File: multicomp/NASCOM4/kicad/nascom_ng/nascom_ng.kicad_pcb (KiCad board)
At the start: 2 copper layers, 170 x 145 mm, 113 parts, among them J1 Conn_02x14_Even_Odd, J10 Conn_01x03_Male, J11 Conn_02x02_Odd_Even, J12 Conn_02x01, J13 Conn_02x02_Odd_Even, J14 Conn_02x08_Odd_Even, J15 Conn_01x04_Male, J16 Conn_01x04_Male, J17 Conn_01x04_Male, J18 Conn_01x04_Male, J2 Conn_02x14_Even_Odd, J3 Conn_02x14_Even_Odd, J4 Conn_02x14_Even_Odd, J5 DB15_Female_HighDensity, J6 DB15_Female_HighDensity, J7 Conn_02x17_Odd_Even, J8 Conn_01x06, J9 Mini-DIN_6pins_ver2, SW1 SW_Push, SW2 SW_Push, SW3 SW_Push, U1 Z80PIO, U10 74HCT244, U11 74LVC244, U12 74LVC244, U13 Z80CTC, U14 74LS38, U15 74LS174, U16 74HCT10, U17 74HCT123, U2 WD2797, U3 74LS06, U4 AS6C4008-55PCN, U5 AS6C4008-55PCN, U6 74LVC245, U7 74LVC244, U8 74LS367, U9 74HCT123

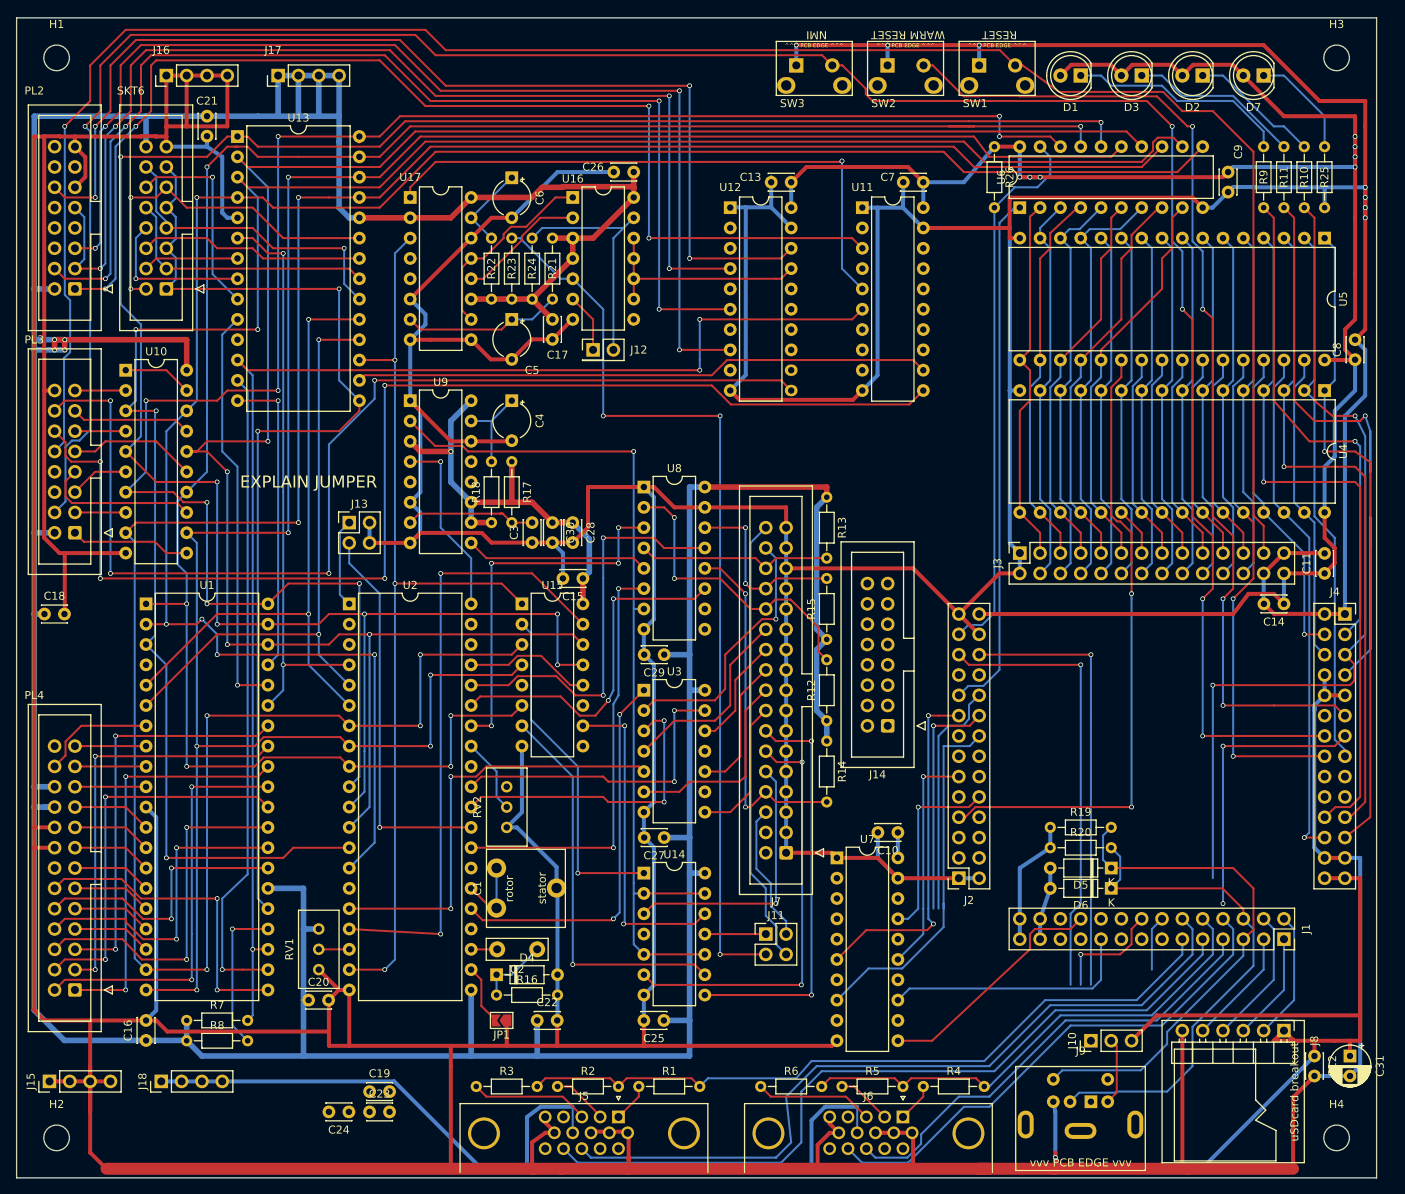
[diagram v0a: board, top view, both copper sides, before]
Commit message: All nets routed, ref designators resequenced, nearly finished!
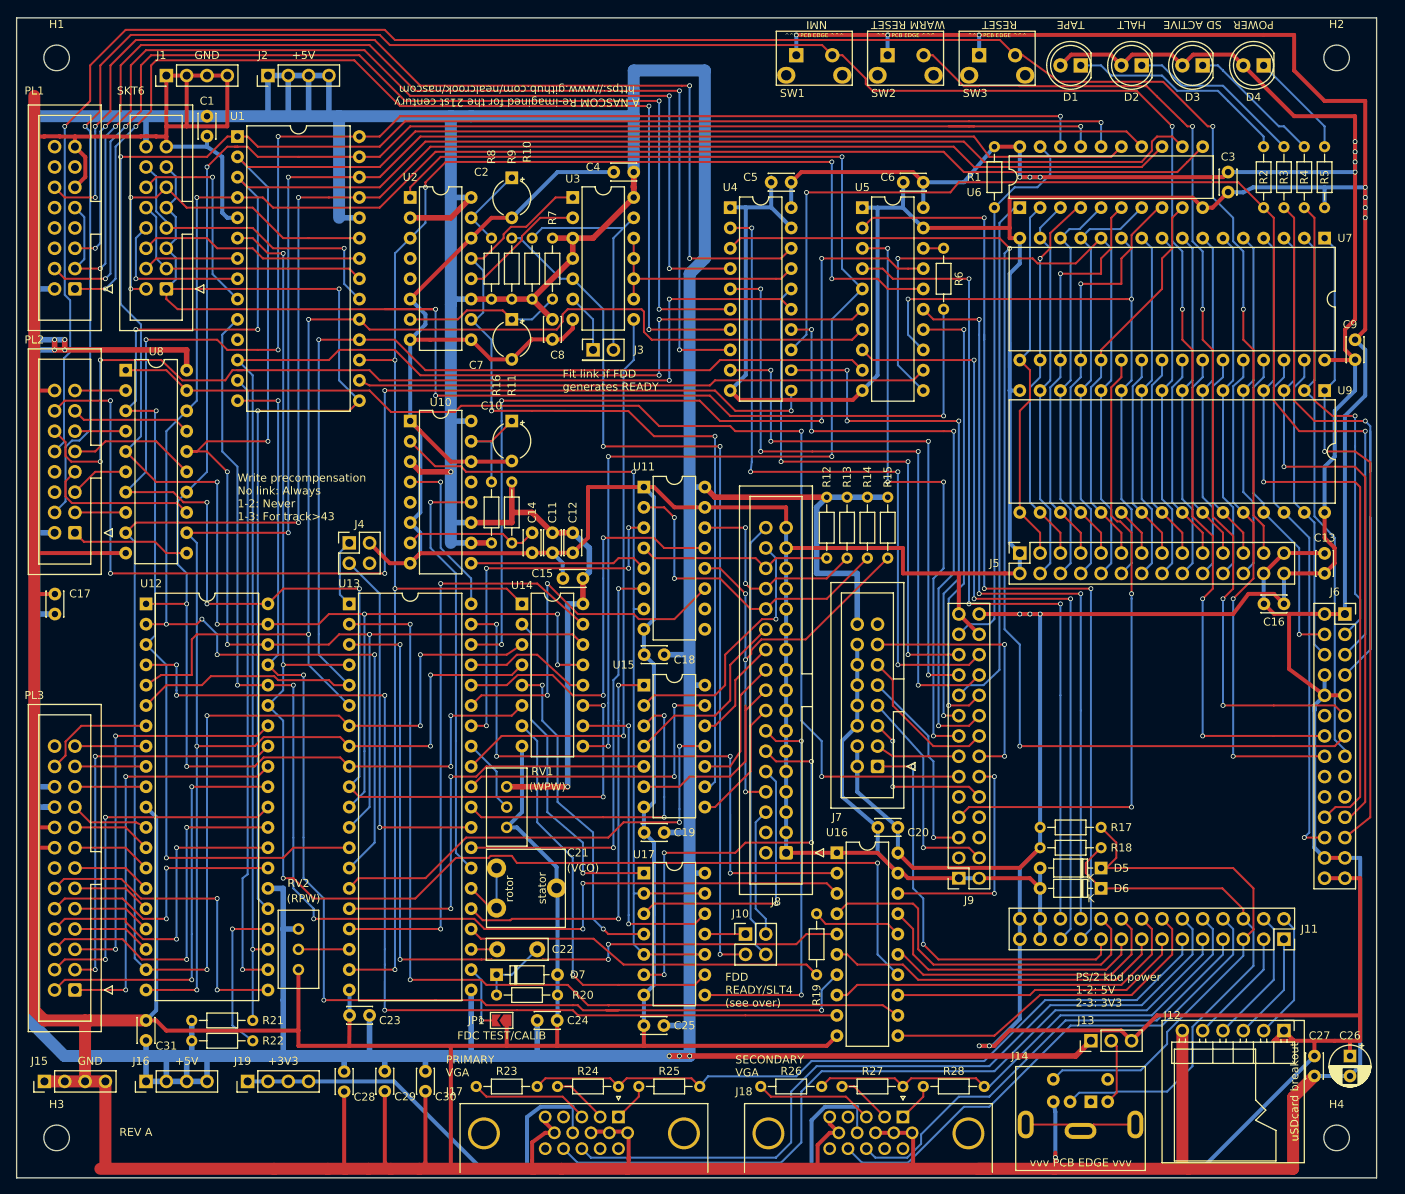
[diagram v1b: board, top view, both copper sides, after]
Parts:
- removed the C14 at (185.4, 95.2)
- removed the C4 at (88.9, 69.8)
- removed the C6 at (88.9, 42.0)
- removed the J14 at (135.9, 110.5)
- removed the R17 at (88.9, 77.5)
- removed the R18 at (86.4, 85.1)
- removed the RV1 at (64.8, 135.9)
- removed the U3 at (105.4, 106.0)
- removed the U7 at (129.5, 127.0)
- removed the U9 at (76.2, 69.8)
- added C10: 1u, Capacitor_THT:CP_Radial_Tantal_D4.5mm_P5.00mm, F.Cu at (88.9, 72.4)
- added C16: 0.1u, Capacitor_THT:C_Disc_D3.0mm_W2.0mm_P2.50mm, F.Cu at (185.4, 95.2)
- added C2: 47u, Capacitor_THT:CP_Radial_Tantal_D4.5mm_P5.00mm, F.Cu at (88.9, 42.0)
- added J16: Conn_01x04_Male, Connector_PinHeader_2.54mm:PinHeader_1x04_P2.54mm_Vertical, F.Cu at (43.2, 154.9)
- added J7: Conn_02x08_Odd_Even, Connector_IDC:IDC-Header_2x08_P2.54mm_Vertical, F.Cu at (134.6, 115.6)
- added R11: 5k6, Resistor_THT:R_Axial_DIN0204_L3.6mm_D1.6mm_P7.62mm_Horizontal, F.Cu at (88.9, 80.0)
- added R16: 100k, Resistor_THT:R_Axial_DIN0204_L3.6mm_D1.6mm_P7.62mm_Horizontal, F.Cu at (86.4, 87.6)
- added R19: 33R, Resistor_THT:R_Axial_DIN0204_L3.6mm_D1.6mm_P7.62mm_Horizontal, F.Cu at (127.0, 134.0)
- added R6: 33R, Resistor_THT:R_Axial_DIN0204_L3.6mm_D1.6mm_P7.62mm_Horizontal, F.Cu at (142.9, 50.8)
- added RV2: 50k, Potentiometer_THT:Potentiometer_Bourns_3296W_Vertical, F.Cu at (62.2, 135.9)
- added U10: 74HCT123, Package_DIP:DIP-16_W7.62mm, F.Cu at (76.2, 72.4)
- added U15: 74LS06, Package_DIP:DIP-14_W7.62mm, F.Cu at (105.4, 105.4)
- added U16: 74LVC244, Package_DIP:DIP-20_W7.62mm, F.Cu at (129.5, 126.4)
- moved R15 31.4 mm to (135.9, 81.9)
- moved R14 28.4 mm to (133.3, 81.9), turned to 270 degrees
- moved R13 18.0 mm to (130.8, 81.9), turned to 270 degrees
- moved J19 10.8 mm to (55.9, 154.9)
- moved C30 8.64 mm to (78.1, 153.7), turned to 270 degrees
- moved C23 7.85 mm to (71.1, 146.7), turned to 180 degrees
- moved C28 5.07 mm to (67.9, 153.7), turned to 270 degrees
- moved C29 3.18 mm to (73.0, 153.7), turned to 270 degrees
- moved J10 2.54 mm to (118.1, 136.5)
- moved J4 2.54 mm to (68.6, 87.6)
- moved C17 1.31 mm to (31.8, 96.5), turned to 90 degrees
- moved D5 1.27 mm to (162.6, 128.3)
- moved D6 1.27 mm to (162.6, 130.8)
- moved R17 1.27 mm to (154.9, 123.2)
- moved R18 1.27 mm to (154.9, 125.7)
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- renumbered C21 to C1, C30 to C11, C28 to C12, C11 to C13, C3 to C14, C18 to C17, C29 to C18, C27 to C19, C10 to C20, C1 to C21, C2 to C22, C20 to C23, C22 to C24, C31 to C26, C12 to C27, C24 to C28, C19 to C29, C9 to C3, C23 to C30, C16 to C31, C26 to C4, C13 to C5, C7 to C6, C5 to C7, C17 to C8, C8 to C9, D3 to D2, D2 to D3, D7 to D4, D4 to D7, H3 to H2, H2 to H3, J16 to J1, J11 to J10, J1 to J11, J8 to J12, J10 to J13, J9 to J14, J5 to J17, J6 to J18, J18 to J19, J17 to J2, J12 to J3, J13 to J4, J3 to J5, J4 to J6, J7 to J8, J2 to J9, PL2 to PL1, PL3 to PL2, PL4 to PL3, R26 to R1, R24 to R10, R13 to R12, R15 to R13, R12 to R14, R14 to R15, R19 to R17, R20 to R18, R9 to R2, R16 to R20, R7 to R21, R8 to R22, R3 to R23, R2 to R24, R1 to R25, R6 to R26, R5 to R27, R4 to R28, R11 to R3, R10 to R4, R25 to R5, R21 to R7, R22 to R8, R23 to R9, RV2 to RV1, SW3 to SW1, SW1 to SW3, U13 to U1, U8 to U11, U1 to U12, U2 to U13, U15 to U14, U14 to U17, U17 to U2, U16 to U3, U12 to U4, U11 to U5, U5 to U7, U10 to U8, U4 to U9
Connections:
- net PIN104_RTS renamed ~PIN104_IOBUFOE
- net PIN22_NCIN renamed ~PIN22_IN_READY
- net PIN51_CLK1 renamed ~PIN72_IO_RESET
- net PIN53_CLK4 renamed PIN69_CLK4
- net PIN71_GPIO3 renamed ~PIN71_CTC_CS
- J11 pad 13: PIN57_GPIO4 -> ~PIN57_M1
- J11 pad 14: PIN58_GPIO5 -> ~PIN58_PIO_CS
- J11 pad 15: PIN59_PORT0RD -> ~PIN59_RD
- J11 pad 16: PIN60_GPIO7 -> ~PIN60_WR
- J11 pad 17: ~PIN63_KBDCLK -> ~PIN63_IORQ
- J11 pad 18: ~PIN64_KBDRST -> ~PIN64_FDC_CS
- J11 pad 19: PIN65_CTS -> PIN65_TVVID
- J11 pad 20: PIN52_RXBAUDCLK -> PIN67_CLK1
- J11 pad 22: PIN70_VDUFFD0 -> PIN70_PORTE4_WR
- J4 pad 4: GND -> (no net)
- J9 pad 10: PIN86_SCL -> PIN86_TX
- J9 pad 11: PIN87_CTS -> PIN87_PORT0RD
- J9 pad 12: (no net) -> PIN88_IN_INTRQ
- J9 pad 13: (no net) -> PIN89_IN_NC
- J9 pad 14: PIN90_IN_DRQ -> PIN90_IN_NC
- J9 pad 15: PIN91_IN_INTRQ -> PIN91_IN_DRQ
- J9 pad 16: PIN92_RIO -> PIN92_TVSYNCH
- J9 pad 17: PIN93_RCERST -> PIN93_RXBAUDCLK
- J9 pad 18: PIN94_SDA -> PIN94_TXBAUDCLK
- J9 pad 20: PIN97_RCLK -> ~PIN97_INT
- J9 pad 21: PIN99_RX -> ~PIN99_KBDRST
- J9 pad 22: PIN100_TX -> ~PIN100_KBDCLK
- J9 pad 4: PIN74_TVSYNCH -> PIN74_RX
- J9 pad 5: PIN75_TVVID -> PIN75_RCLK
- R2 pad 2: PIN3_SDACTIVE -> PIN7_TAPE_DRIVE
- R4 pad 2: PIN7_TAPE_DRIVE -> PIN3_SDACTIVE
- U4 pad 12: PIN52_RXBAUDCLK -> PIN93_RXBAUDCLK
- U4 pad 13: DRQ_5V -> PIN7_TAPE_DRIVE
- U4 pad 14: PIN60_GPIO7 -> PIN94_TXBAUDCLK
- U4 pad 15: INTRQ_5V -> ~KBDCLK_5V
- U4 pad 5: PIN91_IN_INTRQ -> ~PIN100_KBDCLK
- U4 pad 7: PIN90_IN_DRQ -> TAPE_DRIVE_5V
- U4 pad 9: ~PIN64_KBDRST -> ~PIN99_KBDRST
- U5 pad 11: ~KBDCLK_5V -> PIN121_A0
- U5 pad 13: PIN94_SDA -> PIN125_A1
- U5 pad 14: PIN57_GPIO4 -> ~PIN97_INT
- U5 pad 15: PIN58_GPIO5 -> PIN70_PORTE4_WR
- U5 pad 16: CLK1_5V -> ~IO_RESET_5V
- U5 pad 17: PIN7_TAPE_DRIVE -> DRQ_5V
- U5 pad 18: CLK4_5V -> Net-(R6-Pad1)
- U5 pad 3: TAPE_DRIVE_5V -> PIN91_IN_DRQ
- U5 pad 7: ~IO_RESET_5V -> A1_5V
- U5 pad 9: ~PIN63_KBDCLK -> A0_5V
- U8 pad 1: PIN59_PORT0RD -> PIN87_PORT0RD
- U8 pad 19: PIN59_PORT0RD -> PIN87_PORT0RD
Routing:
- net +5V: track 630.7 -> 945.3 mm, vias 5 -> 9
- net PIN87_PORT0RD: track 0.00 -> 149.6 mm, vias 0 -> 2
- net CLK4_5V: track 130.0 -> 261.5 mm, vias 2 -> 5
- net ~PIO_CS_5V: track 0.00 -> 129.8 mm, vias 0 -> 4
- net PIN69_CLK4: track 0.00 -> 120.4 mm, vias 0 -> 3
- net ~M1_5V: track 38.6 -> 156.4 mm, vias 1 -> 4
- net GND: track 1537.4 -> 1653.1 mm
- net ~RD_5V: track 72.1 -> 187.5 mm, vias 2 -> 4
- net ~WR_5V: track 0.00 -> 114.8 mm, vias 0 -> 2
- net DRQ_5V: track 0.00 -> 108.9 mm, vias 0 -> 4
- net ~IORQ_5V: track 51.1 -> 156.7 mm, vias 1 -> 5
- net ~PIN72_IO_RESET: track 0.00 -> 105.3 mm, vias 0 -> 3
- net ~PIN22_IN_READY: track 35.5 -> 140.4 mm
- net ~FDC_CS_5V: track 0.00 -> 102.8 mm, vias 0 -> 4
- net ~PIN71_CTC_CS: track 0.00 -> 99.5 mm, vias 0 -> 3
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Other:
- board text added: ""NASCOM 4" - an FPGA-based NASCOM recreation with the functionality of a NASCOM 2 expanded with disks, a MAP80 VFC and a 2 MAP80 256K RAM boards"
- board text added: "(RPW)"
- board text added: "(VCO)"
- board text added: "(WPW)"
- board text added: "+3V3"
- board text added: "+5V"
- board text added: "A NASCOM Re-imagined for the 21st century https://www.github.com/nealcrook/nascom"
- board text added: "FDC TEST/CALIB"
- board text added: "FDD READY/SLT4 (see over)"
- board text added: "FDD READY/SLT4 Teac FD-55: 1-2, 3-4 Pertec FD250: 1-2 Micropolis 1015: 2-3, 1-4"
- board text added: "Fit link if FDD generates READY"
- board text added: "GND"
- board text added: "HALT"
- board text added: "POWER"
- board text added: "PRIMARY VGA"
- board text added: "PS/2 kbd power 1-2: 5V 2-3: 3V3"
- board text added: "REV A"
- board text added: "SD ACTIVE"
- board text added: "SECONDARY VGA"
- board text added: "TAPE"
- board text added: "Write precompensation No link: Always 1-2: Never 1-3: For track>43"
- board text removed: "EXPLAIN JUMPER"

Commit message: Files for REV A release to PCB manufacture
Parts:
- removed the C17 at (31.8, 96.5)
- removed the C30 at (78.1, 153.7)
- removed the U4 at (116.2, 45.7)
- added C16: 0.1u, Capacitor_THT:C_Disc_D3.0mm_W2.0mm_P2.50mm, F.Cu at (31.8, 94.0)
- added C2: 10u, Capacitor_THT:CP_Radial_D5.0mm_P2.50mm, F.Cu at (132.7, 40.0)
- added C20: 10u, Capacitor_THT:CP_Radial_D5.0mm_P2.50mm, F.Cu at (31.8, 100.3)
- added C3: 10u, Capacitor_THT:CP_Radial_D5.0mm_P2.50mm, F.Cu at (193.0, 41.3)
- added U6: 74LVC244, Package_DIP:DIP-20_W7.62mm, F.Cu at (116.2, 45.7)
- added X1: NASCOM-logo, mylib:nascom_logo_tiny, F.Cu at (89.5, 26.7)
- added X2: KiCad-sm-logo, mylib:KiCad-Logo_5mm_SolderMask, F.Cu at (55.2, 162.6)
- C29: value 0.1u -> 10u; footprint Capacitor_THT:C_Disc_D3.0mm_W2.0mm_P2.50mm -> Capacitor_THT:CP_Radial_D5.0mm_P2.50mm
- moved R10 23.3 mm to (132.7, 71.8), turned to 180 degrees
- moved R1 8.89 mm to (181.6, 38.1)
- moved C6 5.08 mm to (118.7, 42.5)
- moved J10 3.81 mm to (118.1, 140.3)
- moved R19 3.42 mm to (123.8, 135.3), turned to 180 degrees
- moved C28 2.58 mm to (110.5, 148.0)
- moved C21 2.54 mm to (110.5, 101.6)
- moved C22 2.54 mm to (134.6, 123.2)
- moved C23 2.54 mm to (110.5, 123.8)
- moved C26 1.27 mm to (71.1, 148.0)
- moved R2 1.27 mm to (184.2, 38.1)
- moved R3 1.27 mm to (186.7, 38.1)
- moved R4 1.27 mm to (189.2, 38.1)
- moved C27 0.64 mm to (92.1, 148.0)
- moved JP1 0.64 mm to (87.6, 148.0)
- renumbered C7 to C10, C9 to C11, C10 to C12, C11 to C13, C12 to C14, C14 to C15, C13 to C17, C15 to C18, C16 to C19, C18 to C21, C20 to C22, C19 to C23, C22 to C24, C21 to C25, C23 to C26, C24 to C27, C25 to C28, C27 to C30, C28 to C31, C26 to C32, C31 to C33, C3 to C4, C4 to C5, C5 to C6, C6 to C7, C2 to C8, C8 to C9, J7 to J11, J13 to J12, J14 to J13, J15 to J14, J16 to J15, J19 to J16, J12 to J19, J8 to J20, SKT6 to J4, J4 to J5, J5 to J6, J6 to J7, J9 to J8, J11 to J9, PL1 to PL2, PL2 to PL3, PL3 to PL4, R5 to R1, R6 to R10, R1 to R5, R7 to R6, R10 to R7, U6 to U2, U2 to U3, U3 to U4
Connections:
- R10 pad 1: Net-(R6-Pad1) -> Net-(R10-Pad1)
- U5 pad 11: PIN121_A0 -> PIN69_CLK4
- U5 pad 18: Net-(R6-Pad1) -> A0_5V
- U5 pad 2: PIN69_CLK4 -> PIN121_A0
- U5 pad 9: A0_5V -> Net-(R10-Pad1)
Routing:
- net GND: track 1653.1 -> 1773.4 mm, vias 8 -> 5
- net CLK4_5V: track 261.5 -> 230.4 mm, vias 5 -> 4
- net PIN69_CLK4: track 120.4 -> 90.1 mm
- net A0_5V: track 142.7 -> 160.8 mm, vias 1 -> 2
- net +5V: track 945.3 -> 931.2 mm
- net CLK1_5V: track 45.4 -> 34.2 mm
- net Net-(D4-Pad1): track 13.3 -> 24.0 mm
- net PIN121_A0: track 88.8 -> 79.2 mm, vias 1 -> 2
- net Net-(R10-Pad1): track 0.00 -> 7.51 mm
- net Net-(U13-Pad30): track 40.4 -> 35.3 mm
- net +3V3: track 613.3 -> 617.2 mm, vias 12 -> 13
- net ~DRIVE_READY: track 113.5 -> 117.3 mm
- net /nascom_ng_fdc/SPACE_READY: track 54.9 -> 58.8 mm
- net /nascom_ng_fdc/ISLT3: track 16.3 -> 20.1 mm
- net ~M1_5V: track 156.4 -> 153.7 mm
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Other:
- board text added: ""EP2C5T144C8N mini board" Altara FPGA"
- board text added: ""NASCOM 4" - an FPGA-based NASCOM recreation with the functionality of a NASCOM 2 expanded with RAM (4 MAP80 256K boards), disks and 80-col video (a MAP80 VFC)"
- board text added: "1"
- board text added: "2"
- board text added: "3"
- board text added: "4"
- board text added: "74HCT10"
- board text added: "74HCT123"
- board text added: "74LS06"
- board text added: "74LS174"
- board text added: "74LS367"
- board text added: "74LS38"
- board text added: "74LVC244"
- board text added: "74LVC245"
- board text added: "AS6C4008"
- board text added: "AS6C4008 (optional)"
- board text added: "CLK1"
- board text added: "CLK4"
- board text added: "CTC"
- board text added: "EXPANSION/DEBUG"
- board text added: "FLOPPY DISKS"
- board text added: "KBD ONLY"
- board text added: "NASCOM 4 REV A"
- board text added: "PORTS"
- board text added: "READ H/BOOK!"
- board text added: "SERIAL"
- board text added: "Set grid to 1.0mm for edge cuts and holes Set grid to 25mils for routing; tracks are 0.25mm with 0.2mm spacing Change IC pads to oval, 1.6mm x 1.439mm to get 2 tracks through"
- board text added: "WD2797 FDC"
- board text added: "Z80-CTC"
- board text added: "Z80-PIO"
- board text removed: ""NASCOM 4" - an FPGA-based NASCOM recreation with the functionality of a NASCOM 2 expanded with disks, a MAP80 VFC and a 2 MAP80 256K RAM boards"
- board text removed: "REV A"
- board text removed: "Set grid to 1.0mm for edge cuts and holes Set grid to 25mils for routing; tracks are 0.25mm with 0.2mm spacing Change IC holes to oval, 1.6mm x 1.439mm to get 2 tracks through"

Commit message: Add REVB data-base: schematics, pcb and manufacturing files
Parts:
- added J100: Conn_01x01_Male, Connector_PinHeader_2.54mm:PinHeader_1x01_P2.54mm_Vertical, F.Cu at (146.7, 148.0)
- added R100: 10k, Resistor_THT:R_Axial_DIN0204_L3.6mm_D1.6mm_P7.62mm_Horizontal, F.Cu at (154.9, 109.2)
- added R101: 10k, Resistor_THT:R_Axial_DIN0204_L3.6mm_D1.6mm_P7.62mm_Horizontal, F.Cu at (154.9, 111.8)
- added R102: 10k, Resistor_THT:R_Axial_DIN0204_L3.6mm_D1.6mm_P7.62mm_Horizontal, F.Cu at (113.0, 45.7)
- moved R1 7.62 mm to (189.2, 38.1)
- moved R2 2.54 mm to (181.6, 38.1)
- moved R3 2.54 mm to (184.2, 38.1)
- moved R4 2.54 mm to (186.7, 38.1)
- moved D1 1.27 mm to (160.0, 26.7)
- moved D2 1.27 mm to (167.6, 26.7)
- moved D3 1.27 mm to (175.3, 26.7)
- moved D4 1.27 mm to (182.9, 26.7)
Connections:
- J13 pad 1: (no net) -> PIN45_KDAT
- J13 pad 2: PIN45_KDAT -> (no net)
- J13 pad 3: Net-(J12-Pad2) -> GND
- J13 pad 4: GND -> Net-(J12-Pad2)
- J13 pad 5: (no net) -> PIN44_KCLK
- J13 pad 6: PIN44_KCLK -> (no net)
- J7 pad 11: PIN18_IN_WARMRST -> (no net)
- J7 pad 12: (no net) -> PIN18_IN_WARMRST
- J8 pad 3: (no net) -> PIN144_RST
- U6 pad 11: ~KBDRST_5V -> ~PIN99_KBDRST
- U6 pad 15: ~KBDCLK_5V -> ~PIN100_KBDCLK
- U6 pad 5: ~PIN100_KBDCLK -> ~KBDCLK_5V
- U6 pad 9: ~PIN99_KBDRST -> ~KBDRST_5V
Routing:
- net PIN144_RST: track 254.1 -> 337.1 mm, vias 3 -> 6
- net GND: track 1773.4 -> 1803.6 mm, vias 5 -> 8
- net PIN21_IN_NMI: track 295.3 -> 315.2 mm, vias 5 -> 6
- net PIN18_IN_WARMRST: track 128.6 -> 147.1 mm, vias 4 -> 5
- net ~PIN99_KBDRST: track 66.7 -> 56.5 mm, vias 4 -> 3
- net Net-(D4-Pad1): track 24.0 -> 14.1 mm
- net ~KBDRST_5V: track 140.6 -> 130.9 mm, vias 5 -> 4
- net ~KBDCLK_5V: track 120.9 -> 129.2 mm
- net PIN44_KCLK: track 67.1 -> 60.3 mm
- net RX_5V: track 138.4 -> 133.1 mm
- net PIN125_A1: track 79.1 -> 74.9 mm
- net +3V3: track 617.2 -> 620.0 mm
- net PIN45_KDAT: track 66.0 -> 63.4 mm
- net PIN88_IN_INTRQ: track 28.6 -> 31.1 mm
- net ~PIN100_KBDCLK: track 81.2 -> 78.6 mm
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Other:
- board text added: "74HCT244"
- board text added: "NASCOM 4 REV B"
- board text removed: "NASCOM 4 REV A"
